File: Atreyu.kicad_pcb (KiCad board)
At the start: 2 copper layers, 122 parts, among them SW1 SW_Push, U1 Elite-C

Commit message: Checkpoint commit.
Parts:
- D1, D10, D11, D12, D13, D14, D15, D16, D17, D18, D19, D2, D20, D21, D22, D23, D24, D25, D26, D27, D28, D29, D3, D30, D31, D32, D33, D34, D35, D36, D37, D38, D39, D4, D40, D41, D42, D43, D44, D45, D46, D47, D48, D49, D5, D50, D51, D52, D53, D54, D55, D56, D57, D58, D59, D6, D60, D7, D8, D9: moved to B.Cu
- moved SW1 194.6 mm to (167.4, -13.2)
- moved D57 132.5 mm to (181.3, 154.4), turned to 180 degrees
- moved D58 132.5 mm to (181.3, 151.4), turned to 180 degrees
- moved D56 122.9 mm to (176.5, 154.1), turned to 180 degrees
- moved D59 113.4 mm to (171.7, 151.1), turned to 180 degrees
- moved D60 113.4 mm to (171.7, 148.1), turned to 180 degrees
- moved D54 113.3 mm to (171.7, 154.1), turned to 180 degrees
- moved D52 103.8 mm to (166.9, 151.1), turned to 180 degrees
- moved D53 103.8 mm to (166.9, 148.1), turned to 180 degrees
- moved D42 103.7 mm to (166.9, 155.1), turned to 180 degrees
- moved D45 94.2 mm to (162.1, 152.1), turned to 180 degrees
- moved D51 94.2 mm to (162.1, 149.1), turned to 180 degrees
- moved D55 94.2 mm to (162.1, 146.1), turned to 180 degrees
- moved D41 94.0 mm to (162.0, 155.1), turned to 180 degrees
- moved D44 84.6 mm to (157.3, 152.1), turned to 180 degrees
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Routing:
- net ROW4: track 0.00 -> 147.9 mm
- net COL4: track 0.00 -> 109.2 mm
- net ROW1: track 0.00 -> 104.8 mm
- net ROW3: track 0.00 -> 104.7 mm
- net ROW2: track 0.00 -> 103.8 mm
- net COL3: track 0.00 -> 101.1 mm
- net COL2: track 0.00 -> 94.7 mm
- net COL1: track 0.00 -> 90.8 mm
- net COL0: track 0.00 -> 85.1 mm
- net COL5: track 0.00 -> 82.3 mm
- net ROW0: track 65.7 -> 103.4 mm
- net Net-(D16-Pad2): track 0.00 -> 14.3 mm
- net Net-(D23-Pad2): track 0.00 -> 13.3 mm
- net Net-(D6-Pad2): track 0.00 -> 13.3 mm
- net Net-(D18-Pad2): track 0.00 -> 13.3 mm
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
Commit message: Last update.
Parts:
- removed the MX25 at (106.4, 95.8)
- added MX25: MX-NoLED, MX_Alps_Hybrid:MX-1U-NoLED, F.Cu at (111.0, 90.7)
- added MX25: MX-NoLED, MX_Alps_Hybrid:MX-1U-NoLED, F.Cu at (106.4, 98.6)
- added MX40: MX-NoLED, MX_Alps_Hybrid:MX-1U-NoLED, F.Cu at (155.7, 90.7)
- moved U1 43.8 mm to (178.8, -39.4)
- moved SW1 21.3 mm to (154.2, -30.0)
- moved D25 16.2 mm to (103.1, 84.3)
- moved MX10 2.79 mm to (42.9, 86.6)
- moved MX40 2.79 mm to (160.3, 98.6), turned to 300 degrees
- moved MX55 2.79 mm to (223.8, 86.6)
- moved D10 2.79 mm to (50.3, 77.7)
- moved D15 2.79 mm to (69.8, 75.4)
- moved D20 2.79 mm to (93.7, 81.3)
- moved MX15 2.79 mm to (62.0, 84.8)
- moved MX20 2.79 mm to (84.6, 87.9)
- moved MX45 2.79 mm to (182.1, 87.9)
- moved MX50 2.79 mm to (204.7, 84.8)
- moved D4 2.54 mm to (4.04, 66.0)
- moved D5 2.54 mm to (21.6, 86.6)
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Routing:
- net COL4: track 109.2 -> 58.6 mm
- net Net-(D25-Pad2): track 5.00 -> 22.4 mm
- net ROW1: track 104.8 -> 108.9 mm
- net ROW3: track 104.7 -> 108.8 mm
- net ROW0: track 103.4 -> 106.4 mm
- net ROW2: track 103.8 -> 106.9 mm
- net ROW4: track 147.9 -> 145.7 mm
- net COL3: track 101.1 -> 102.9 mm
- net COL1: track 90.8 -> 92.5 mm
- net COL5: track 82.3 -> 83.5 mm
- net COL2: track 94.7 -> 95.8 mm

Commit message: Tracks routed and sides aligned with the edge cuts layer.
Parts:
- removed the MX40 at (155.7, 90.7)
- removed the MX40 at (160.3, 98.6)
- added MX40: MX-NoLED, kbd:CherryMX_Hotswap, F.Cu at (216.3, 149.2)
- added MX62: MX-NoLED, kbd:CherryMX_Hotswap, F.Cu at (223.3, 155.0)
- D1, D10, D11, D12, D13, D14, D15, D16, D17, D18, D19, D2, D20, D21, D22, D23, D24, D25, D26, D27, D28, D29, D3, D30, D31, D32, D33, D34, D35, D36, D37, D38, D39, D4, D40, D41, D42, D43, D44, D45, D46, D47, D48, D49, D5, D50, D51, D52, D53, D54, D55, D56, D57, D58, D59, D6, D60, D7, D8, D9: footprint Capacitor_SMD:C_0805_2012Metric_Pad1.18x1.45mm_HandSolder -> Keebio-Parts:D3_hybrid_common_hole
- MX1, MX10, MX11, MX12, MX13, MX14, MX15, MX16, MX17, MX18, MX19, MX2, MX20, MX21, MX22, MX23, MX24, MX25, MX26, MX27, MX28, MX29, MX3, MX30, MX31, MX32, MX33, MX34, MX35, MX36, MX37, MX38, MX39, MX4, MX41, MX42, MX43, MX44, MX45, MX46, MX47, MX48, MX49, MX5, MX50, MX51, MX52, MX53, MX54, MX55, MX56, MX57, MX58, MX59, MX6, MX60, MX7, MX8, MX9: footprint MX_Alps_Hybrid:MX-1U-NoLED -> kbd:CherryMX_Hotswap
- MX61: renamed from MX25; footprint MX_Alps_Hybrid:MX-1U-NoLED -> kbd:CherryMX_Hotswap
- moved D56 157.4 mm to (294.1, 49.5), turned to 20 degrees
- moved D57 153.0 mm to (295.1, 52.1), turned to 20 degrees
- moved D59 150.3 mm to (308.1, 87.9), turned to 20 degrees
- moved D51 147.9 mm to (275.1, 53.7), turned to 20 degrees
- moved D52 144.5 mm to (276.1, 56.3), turned to 20 degrees
- moved D58 142.2 mm to (307.2, 85.3), turned to 20 degrees
- moved D46 139.1 mm to (255.2, 55.3), turned to 20 degrees
- moved D53 134.6 mm to (288.2, 89.5), turned to 20 degrees
- moved D47 134.4 mm to (256.1, 57.9), turned to 20 degrees
- moved D54 132.8 mm to (289.1, 92.1), turned to 20 degrees
- moved D48 132.5 mm to (268.2, 91.1), turned to 20 degrees
- moved U1 131.3 mm to (185.3, 91.8)
- moved D60 131.1 mm to (300.2, 121.9), turned to 20 degrees
- moved D49 127.9 mm to (269.1, 93.7), turned to 20 degrees
- moved D41 121.0 mm to (236.1, 59.5), turned to 20 degrees
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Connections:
- U1 pad 21: Net-(U1-Pad21) -> unconnected-(U1-Pad21)
- U1 pad 23: Net-(U1-Pad23) -> unconnected-(U1-Pad23)
- U1 pad 24: Net-(U1-Pad24) -> unconnected-(U1-Pad24)
- U1 pad 25: Net-(U1-Pad25) -> unconnected-(U1-Pad25)
- U1 pad 26: Net-(U1-Pad26) -> unconnected-(U1-Pad26)
- U1 pad 27: Net-(U1-Pad27) -> unconnected-(U1-Pad27)
- U1 pad 28: Net-(U1-Pad28) -> unconnected-(U1-Pad28)
- U1 pad 29: Net-(U1-Pad29) -> unconnected-(U1-Pad29)
- U1 pad 3: Net-(U1-Pad3) -> unconnected-(U1-Pad3)
- U1 pad 4: Net-(U1-Pad4) -> unconnected-(U1-Pad4)
- U1 pad 5: Net-(U1-Pad5) -> unconnected-(U1-Pad5)
- U1 pad 6: Net-(U1-Pad6) -> unconnected-(U1-Pad6)
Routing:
- net COL4: track 58.6 -> 278.8 mm
- net ROW5: track 0.00 -> 128.6 mm
- net ROW8: track 0.00 -> 105.5 mm
- net ROW6: track 0.00 -> 105.5 mm
- net COL3: track 102.9 -> 208.0 mm
- net ROW9: track 0.00 -> 105.0 mm
- net ROW7: track 0.00 -> 105.0 mm
- net COL0: track 85.1 -> 188.8 mm
- net COL2: track 95.8 -> 193.9 mm
- net COL1: track 92.5 -> 190.5 mm
- net COL5: track 83.5 -> 176.3 mm
- net Net-(D40-Pad2): track 0.00 -> 31.2 mm
- net Net-(D48-Pad2): track 0.00 -> 19.8 mm
- net Net-(D36-Pad2): track 0.00 -> 19.0 mm
- net Net-(D58-Pad2): track 0.00 -> 19.0 mm
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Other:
- board outline added: 296.2 x 145.9 mm
- net class Default removed

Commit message: Completed v0.1.
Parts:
- SW1: footprint random-keyboard-parts:SKQG-1155865 -> kbd:ResetSW_1side
- moved SW1 12.3 mm to (175.6, 39.9), turned to -7 degrees
- moved D25 8.33 mm to (158.1, 129.3)
- moved MX28 8.33 mm to (156.4, 96.0)
- moved D29 8.33 mm to (159.8, 108.8)
- moved D24 8.33 mm to (142.5, 100.1)
- moved MX7 8.33 mm to (89.3, 54.5)
- moved MX20 8.33 mm to (136.1, 133.3)
- moved MX17 8.33 mm to (128.3, 60.3)
- moved MX16 8.33 mm to (134.8, 42.4)
- moved D5 8.33 mm to (75.1, 115.0)
- moved MX10 8.33 mm to (97.3, 117.8)
- moved MX15 8.33 mm to (115.9, 122.7)
- moved MX21 8.33 mm to (152.1, 51.4)
- moved D11 8.33 mm to (120.2, 48.4)
- moved MX8 8.33 mm to (82.8, 72.4)
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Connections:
- U1 pad 13: ROW9 -> ROW5
- U1 pad 14: ROW8 -> ROW6
- U1 pad 16: ROW6 -> ROW8
- U1 pad 17: ROW5 -> ROW9
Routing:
- net COL0: track 188.8 -> 451.3 mm, vias 0 -> 1
- net COL1: track 190.5 -> 426.5 mm, vias 0 -> 1
- net COL2: track 193.9 -> 387.6 mm, vias 0 -> 1
- net COL3: track 208.0 -> 352.1 mm, vias 0 -> 1
- net COL4: track 278.8 -> 386.2 mm, vias 0 -> 1
- net COL5: track 176.3 -> 249.1 mm, vias 0 -> 1
- net Net-(SW1-Pad1): track 0.00 -> 44.5 mm
- net ROW6: track 105.5 -> 132.7 mm
- net ROW7: track 105.0 -> 131.9 mm
- net ROW3: track 106.1 -> 132.8 mm
- net ROW2: track 104.9 -> 131.4 mm
- net ROW8: track 105.5 -> 128.0 mm
- net ROW1: track 105.4 -> 127.5 mm
- net ROW9: track 105.0 -> 127.1 mm
- net ROW0: track 105.0 -> 126.8 mm
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
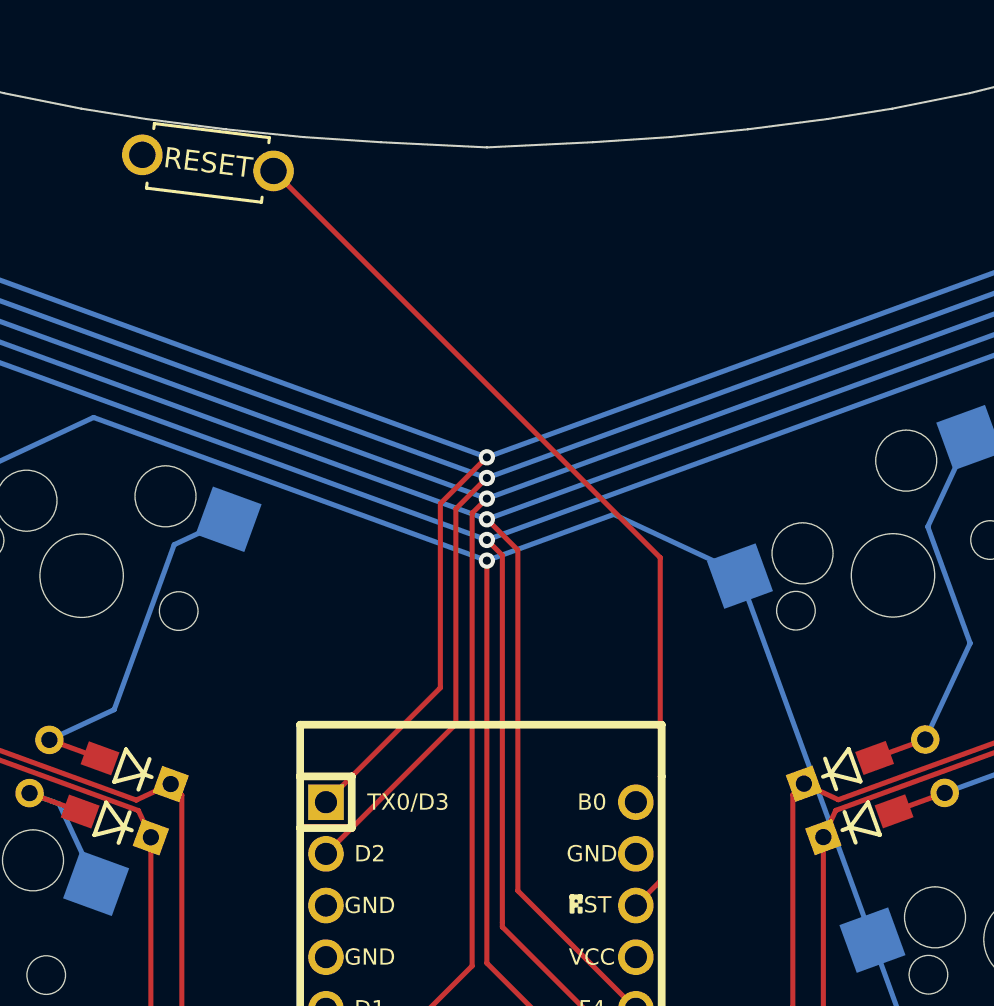
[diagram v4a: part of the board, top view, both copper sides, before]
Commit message: Moved reset button to the right and added SVG file with contour.
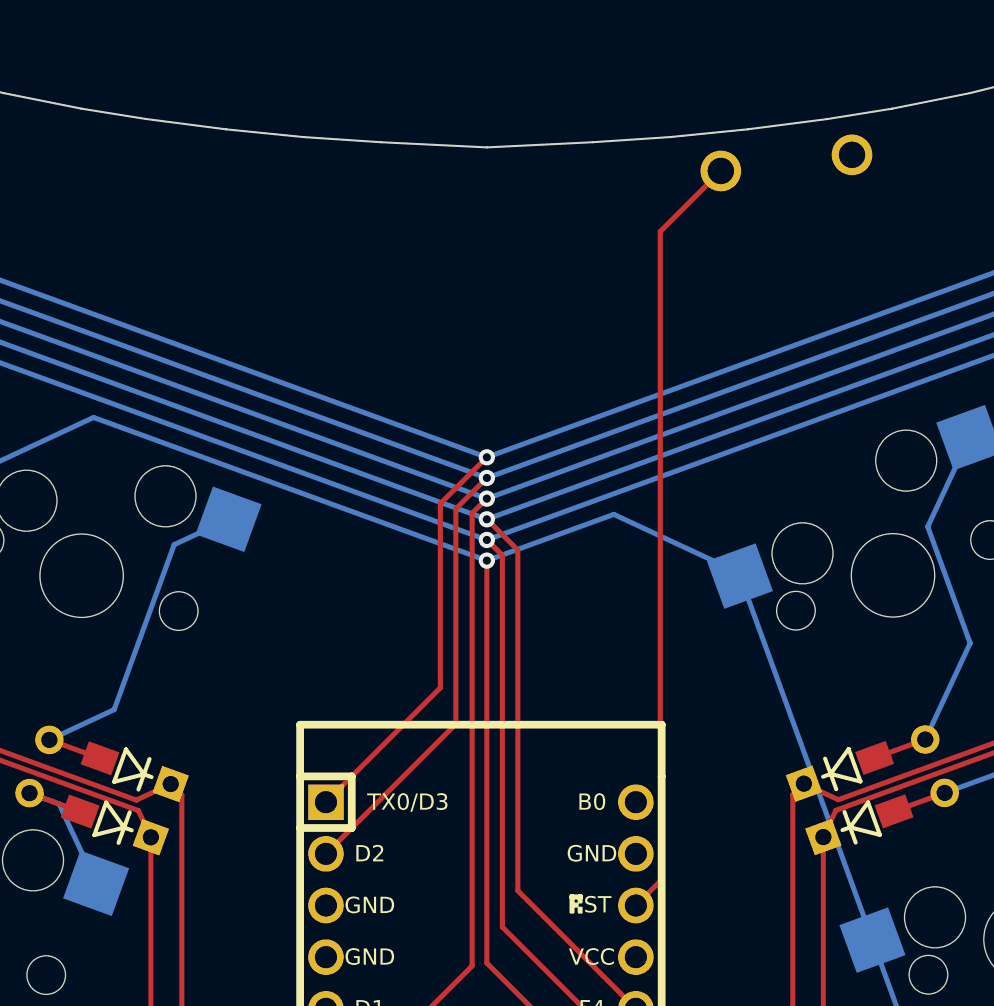
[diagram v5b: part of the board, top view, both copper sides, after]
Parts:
- SW1: moved to B.Cu
- moved SW1 28.4 mm to (204.1, 39.9), turned to -173 degrees
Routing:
- net Net-(SW1-Pad1): track 44.5 -> 37.9 mm
